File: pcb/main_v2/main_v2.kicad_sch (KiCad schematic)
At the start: 9 parts, among them J101 Conn_Coaxial, J102 Conn_Coaxial, J103 Conn_Coaxial, J104 Conn_Coaxial, J105 CONMHF1-SMD-T

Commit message: finished layout
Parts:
- removed J105: CONMHF1-SMD-T, CONMHF1SMDT, symbol My Symbols:CONMHF1-SMD-T
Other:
- note removed: "todo: CONMHF1-SMD-T für rf debugging"
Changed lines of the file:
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@@
 	(generator_version "10.0")
 	(paper "A4")
-	(text "todo: CONMHF1-SMD-T\n für rf debugging"
-		(exclude_from_sim no)
-		(at 37.592 61.214 0)
-		(effects
-			(font
-				(size 1.27 1.27)
-			)
-		)
-	)
 	(text "RFSOC:\nhttps://www.realdigital.org/downloads/15456c97a4fe5a1ee66208c5aa3894bb.pdf\n\nADC:\nmax input power: 14.6 dBm\nattenuation range: 27 dB\ninput bandwith: 6 GHz\n\nDAC:\nMax output power: -18.5 to 6.5 dBm\ncurrent max: 40.5 mA\n"
 		(exclude_from_sim no)
@@
 					(unit 1)
 				)
-			)
-		)
-	)
-	(symbol
-		(lib_id "My Symbols:CONMHF1-SMD-T")
-		(at 90.17 100.33 0)
-		(unit 1)
-		(body_style 1)
-		(exclude_from_sim no)
-		(in_bom yes)
-		(on_board yes)
-		(in_pos_files yes)
-		(dnp no)
-		(fields_autoplaced yes)
-		(property "Reference" "J105"
-			(at 125.73 93.9098 0)
-			(show_name no)
-			(do_not_autoplace no)
-			(effects
-				(font
-					(size 1.27 1.27)
-				)
-			)
-		)
-		(property "Value" "CONMHF1-SMD-T"
-			(at 125.73 96.4498 0)
-			(show_name no)
-			(do_not_autoplace no)
-			(effects
-				(font
-					(size 1.27 1.27)
-				)
-			)
-		)
-		(property "Footprint" "CONMHF1SMDT"
-			(at 116.84 185.09 0)
-			(hide yes)
-			(show_name no)
-			(do_not_autoplace no)
-			(effects
-				(font
-					(size 1.27 1.27)
-				)
-				(justify left top)
-			)
-		)
-		(property "Datasheet" "https://www.te.com/commerce/DocumentDelivery/DDEController?Action=srchrtrv&DocNm=conmhf1-smd-g-t-ds&DocType=Data%20Sheet&DocLang=English&PartCntxt=CONMHF1-SMD-T&DocFormat=pdf"
-			(at 116.84 285.09 0)
-			(hide yes)
-			(show_name no)
-			(do_not_autoplace no)
-			(effects
-				(font
-					(size 1.27 1.27)
-				)
-				(justify left top)
-			)
-		)
-		(property "Description" "U.FL (UMCC) Connector Jack, Male Pin 50 Ohms Surface Mount Solder"
-			(at 90.17 100.33 0)
-			(hide yes)
-			(show_name no)
-			(do_not_autoplace no)
-			(effects
-				(font
-					(size 1.27 1.27)
-				)
-			)
-		)
-		(property "Height" "1.31"
-			(at 116.84 485.09 0)
-			(hide yes)
-			(show_name no)
-			(do_not_autoplace no)
-			(effects
-				(font
-					(size 1.27 1.27)
-				)
-				(justify left top)
-			)
-		)
-		(property "Mouser Part Number" "712-CONMHF1-SMD-T"
-			(at 116.84 585.09 0)
-			(hide yes)
-			(show_name no)
-			(do_not_autoplace no)
-			(effects
-				(font
-					(size 1.27 1.27)
-				)
-				(justify left top)
-			)
-		)
-		(property "Mouser Price/Stock" "https://www.mouser.co.uk/ProductDetail/TE-Connectivity-Linx-Technologies/CONMHF1-SMD-T?qs=7D1LtPJG0i2FCBGfMy%252B%252BIw%3D%3D"
-			(at 116.84 685.09 0)
-			(hide yes)
-			(show_name no)
-			(do_not_autoplace no)
-			(effects
-				(font
-					(size 1.27 1.27)
-				)
-				(justify left top)
-			)
-		)
-		(property "Manufacturer_Name" "TE Connectivity"
-			(at 116.84 785.09 0)
-			(hide yes)
-			(show_name no)
-			(do_not_autoplace no)
-			(effects
-				(font
-					(size 1.27 1.27)
-				)
-				(justify left top)
-			)
-		)
-		(property "Manufacturer_Part_Number" "CONMHF1-SMD-T"
-			(at 116.84 885.09 0)
-			(hide yes)
-			(show_name no)
-			(do_not_autoplace no)
-			(effects
-				(font
-					(size 1.27 1.27)
-				)
-				(justify left top)
-			)
-		)
-		(pin "4"
-		)
-		(pin "3"
-		)
-		(pin "1"
-		)
-		(pin "2"
-		)
-		(instances
-			(project "main_v2"
-				(path "/0599865e-4bed-44f1-b46e-4b55335b49b2"
-					(reference "J105")
-					(unit 1)
-				)

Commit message: updated layout
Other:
- note added: "todo: CONMHF1-SMD-T für rf debugging"
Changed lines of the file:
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@@
 	(generator_version "10.0")
 	(paper "A4")
+	(text "todo: CONMHF1-SMD-T\nfür rf debugging"
+		(exclude_from_sim no)
+		(at 37.592 61.214 0)
+		(effects
+			(font
+				(size 1.27 1.27)
+			)
+		)
+	)
 	(text "RFSOC:\nhttps://www.realdigital.org/downloads/15456c97a4fe5a1ee66208c5aa3894bb.pdf\n\nADC:\nmax input power: 14.6 dBm\nattenuation range: 27 dB\ninput bandwith: 6 GHz\n\nDAC:\nMax output power: -18.5 to 6.5 dBm\ncurrent max: 40.5 mA\n"
 		(exclude_from_sim no)

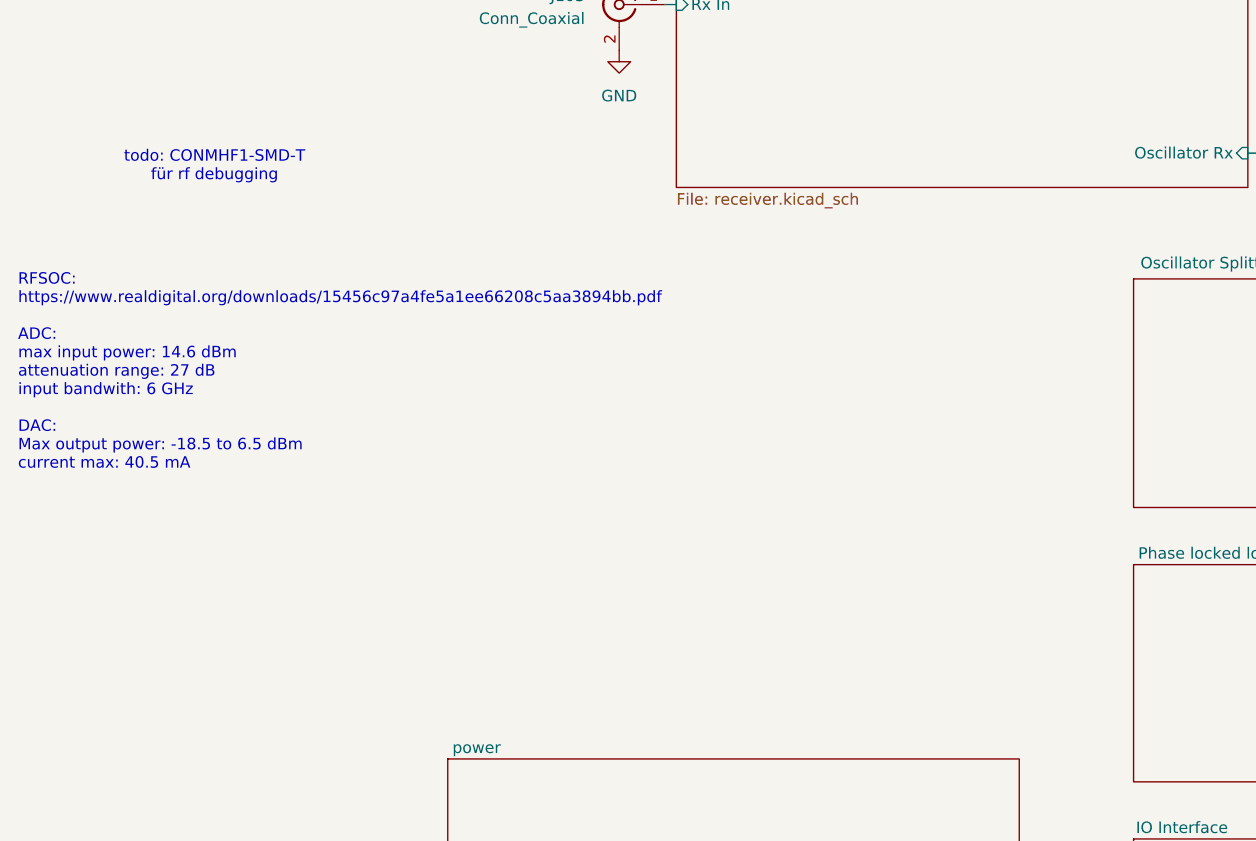
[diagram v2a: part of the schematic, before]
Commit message: updated layout
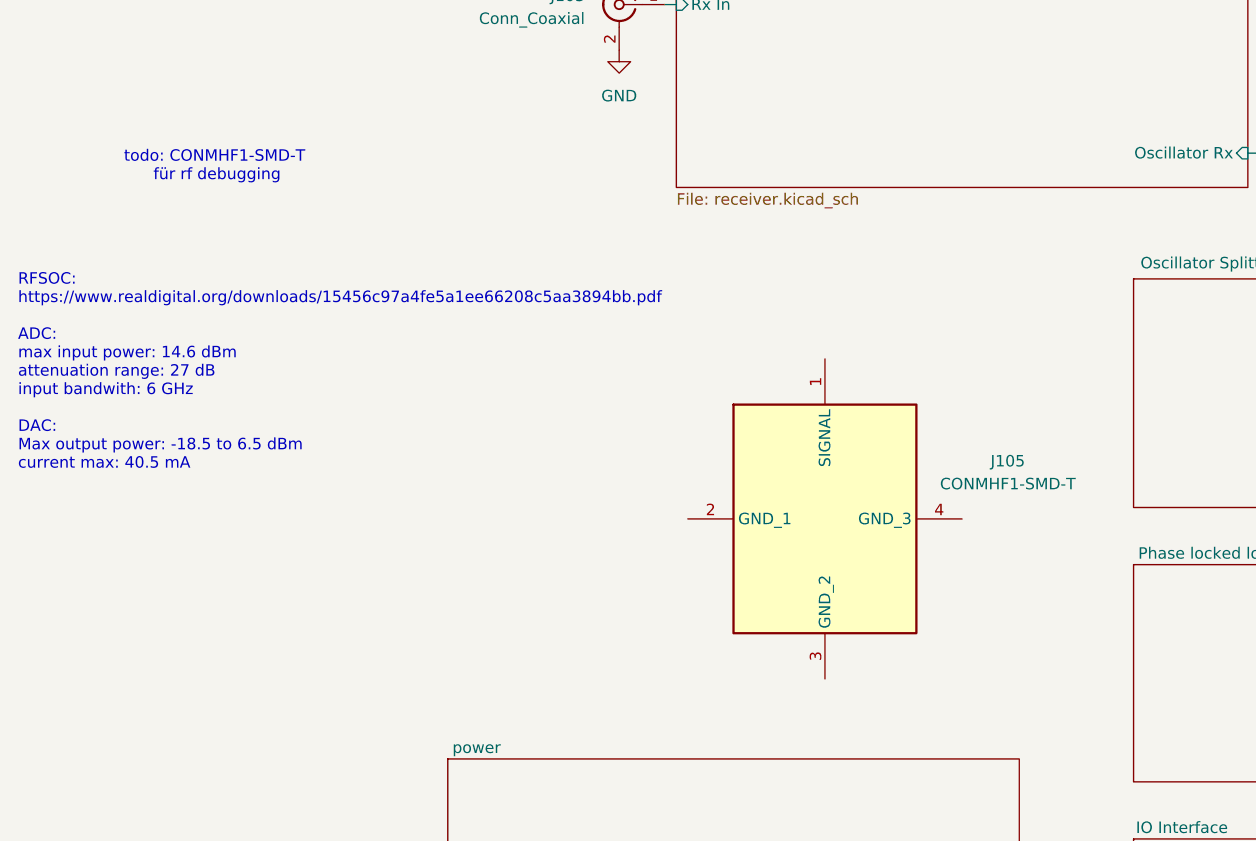
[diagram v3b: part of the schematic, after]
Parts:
- added J105: CONMHF1-SMD-T, CONMHF1SMDT, symbol My Symbols:CONMHF1-SMD-T
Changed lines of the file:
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@@
 	(generator_version "10.0")
 	(paper "A4")
-	(text "todo: CONMHF1-SMD-T\nfür rf debugging"
+	(text "todo: CONMHF1-SMD-T\n für rf debugging"
 		(exclude_from_sim no)
 		(at 37.592 61.214 0)
@@
 					(unit 1)
 				)
+			)
+		)
+	)
+	(symbol
+		(lib_id "My Symbols:CONMHF1-SMD-T")
+		(at 90.17 100.33 0)
+		(unit 1)
+		(body_style 1)
+		(exclude_from_sim no)
+		(in_bom yes)
+		(on_board yes)
+		(in_pos_files yes)
+		(dnp no)
+		(fields_autoplaced yes)
+		(property "Reference" "J105"
+			(at 125.73 93.9098 0)
+			(show_name no)
+			(do_not_autoplace no)
+			(effects
+				(font
+					(size 1.27 1.27)
+				)
+			)
+		)
+		(property "Value" "CONMHF1-SMD-T"
+			(at 125.73 96.4498 0)
+			(show_name no)
+			(do_not_autoplace no)
+			(effects
+				(font
+					(size 1.27 1.27)
+				)
+			)
+		)
+		(property "Footprint" "CONMHF1SMDT"
+			(at 116.84 185.09 0)
+			(hide yes)
+			(show_name no)
+			(do_not_autoplace no)
+			(effects
+				(font
+					(size 1.27 1.27)
+				)
+				(justify left top)
+			)
+		)
+		(property "Datasheet" "https://www.te.com/commerce/DocumentDelivery/DDEController?Action=srchrtrv&DocNm=conmhf1-smd-g-t-ds&DocType=Data%20Sheet&DocLang=English&PartCntxt=CONMHF1-SMD-T&DocFormat=pdf"
+			(at 116.84 285.09 0)
+			(hide yes)
+			(show_name no)
+			(do_not_autoplace no)
+			(effects
+				(font
+					(size 1.27 1.27)
+				)
+				(justify left top)
+			)
+		)
+		(property "Description" "U.FL (UMCC) Connector Jack, Male Pin 50 Ohms Surface Mount Solder"
+			(at 90.17 100.33 0)
+			(hide yes)
+			(show_name no)
+			(do_not_autoplace no)
+			(effects
+				(font
+					(size 1.27 1.27)
+				)
+			)
+		)
+		(property "Height" "1.31"
+			(at 116.84 485.09 0)
+			(hide yes)
+			(show_name no)
+			(do_not_autoplace no)
+			(effects
+				(font
+					(size 1.27 1.27)
+				)
+				(justify left top)
+			)
+		)
+		(property "Mouser Part Number" "712-CONMHF1-SMD-T"
+			(at 116.84 585.09 0)
+			(hide yes)
+			(show_name no)
+			(do_not_autoplace no)
+			(effects
+				(font
+					(size 1.27 1.27)
+				)
+				(justify left top)
+			)
+		)
+		(property "Mouser Price/Stock" "https://www.mouser.co.uk/ProductDetail/TE-Connectivity-Linx-Technologies/CONMHF1-SMD-T?qs=7D1LtPJG0i2FCBGfMy%252B%252BIw%3D%3D"
+			(at 116.84 685.09 0)
+			(hide yes)
+			(show_name no)
+			(do_not_autoplace no)
+			(effects
+				(font
+					(size 1.27 1.27)
+				)
+				(justify left top)
+			)
+		)
+		(property "Manufacturer_Name" "TE Connectivity"
+			(at 116.84 785.09 0)
+			(hide yes)
+			(show_name no)
+			(do_not_autoplace no)
+			(effects
+				(font
+					(size 1.27 1.27)
+				)
+				(justify left top)
+			)
+		)
+		(property "Manufacturer_Part_Number" "CONMHF1-SMD-T"
+			(at 116.84 885.09 0)
+			(hide yes)
+			(show_name no)
+			(do_not_autoplace no)
+			(effects
+				(font
+					(size 1.27 1.27)
+				)
+				(justify left top)
+			)
+		)
+		(pin "4"
+		)
+		(pin "3"
+		)
+		(pin "1"
+		)
+		(pin "2"
+		)
+		(instances
+			(project "main_v2"
+				(path "/0599865e-4bed-44f1-b46e-4b55335b49b2"
+					(reference "J105")
+					(unit 1)
+				)
